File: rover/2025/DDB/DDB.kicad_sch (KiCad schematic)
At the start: 93 parts, among them J1 USB_C_USB4105-GF-A, J2 ETH-RJHSE508104, J3 TerminalBlock, J4 ETH-RJHSE508104, J8 XT30PW-F, SW1 TS09-63-25-WT-160-SMT-TR, SW2 TS09-63-25-WT-160-SMT-TR, U1 ESP32-S3-WROVER, U10 HSS-VN7140ASTR, U11 HSS-VN7140ASTR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

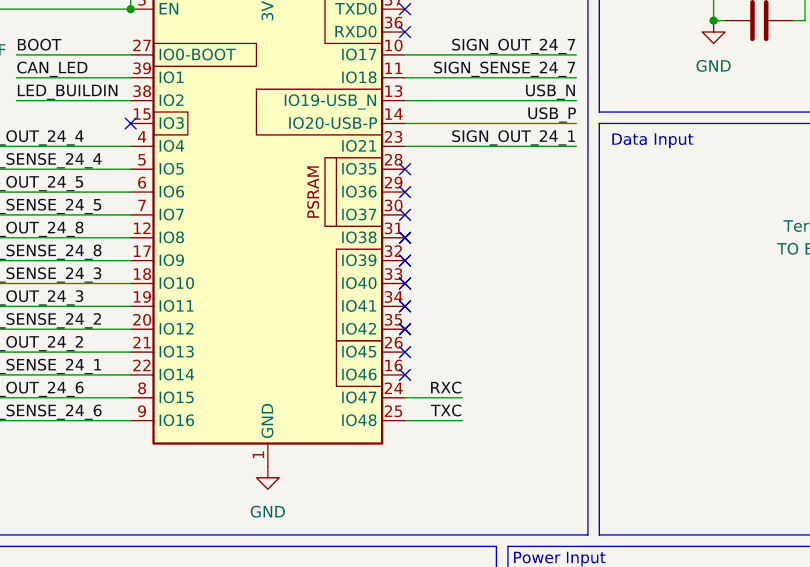
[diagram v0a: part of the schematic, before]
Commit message: Update sch and pcb for correct link
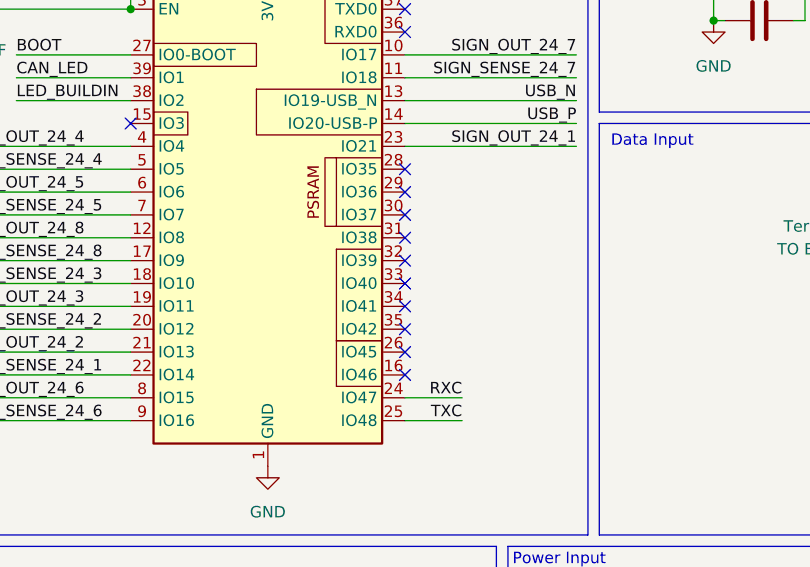
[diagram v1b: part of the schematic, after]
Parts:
- C1: symbol RoverLibrary:C-1uF -> 0_RoverLibrary:C-1uF
- C2: symbol RoverLibrary:C-22uF -> 0_RoverLibrary:C-22uF
- C3, C4, C5, C7: symbol RoverLibrary:C-100nF -> 0_RoverLibrary:C-100nF
- F1, F10, F11, F2, F3, F4, F5, F6, F7, F8: footprint 0_RoverFootprint:FUSE_3568-20 -> RoverFootprint:FUSE_3568-20
- H6, H7: symbol RoverLibrary:MountingHole_Pad -> 0_RoverLibrary:MountingHole_Pad
- R1: symbol RoverLibrary:R-10k -> 0_RoverLibrary:R-10k
- SW1, SW2: symbol RoverLibrary:PushButton-TS09-63-25-WT-160-SMT-TR -> 0_RoverLibrary:PushButton-TS09-63-25-WT-160-SMT-TR
- U1: symbol RoverLibrary:ESP32-S3-WROVER -> 0_RoverLibrary:ESP32-S3-WROVER
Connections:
- no-connect marks 54 -> 49

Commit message: .
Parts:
- U6: value HSS-VN7004SLHTR -> HSS-VN7004SLHTR
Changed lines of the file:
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@@
 	(label "RXC"
 		(at 106.68 72.39 180)
-		(fields_autoplaced yes)
 		(effects
 			(font
@@
 	(label "BOOT"
 		(at 57.15 34.29 0)
-		(fields_autoplaced yes)
 		(effects
 			(font
@@
 	(label "SIGN_SENSE_24_4"
 		(at 50.8 46.99 0)
-		(fields_autoplaced yes)
 		(effects
 			(font
@@
 	(label "CANH"
 		(at 361.95 175.26 180)
-		(fields_autoplaced yes)
 		(effects
 			(font
@@
 	(label "CANL"
 		(at 350.52 39.37 0)
-		(fields_autoplaced yes)
 		(effects
 			(font
@@
 	(label "SIGN_OUT_24_2"
 		(at 20.32 212.09 0)
-		(fields_autoplaced yes)
 		(effects
 			(font
@@
 	(label "SIGN_OUT_24_3"
 		(at 20.32 251.46 0)
-		(fields_autoplaced yes)
 		(effects
 			(font
@@
 	(label "CANH"
 		(at 350.52 62.23 0)
-		(fields_autoplaced yes)
 		(effects
 			(font
@@
 	(label "USB_P"
 		(at 119.38 41.91 180)
-		(fields_autoplaced yes)
 		(effects
 			(font
@@
 	(label "SIGN_OUT_24_8"
 		(at 50.8 54.61 0)
-		(fields_autoplaced yes)
 		(effects
 			(font
@@
 	(label "SIGN_OUT_24_6"
 		(at 50.8 72.39 0)
-		(fields_autoplaced yes)
 		(effects
 			(font
@@
 	(label "SIGN_SENSE_24_3"
 		(at 36.83 254 0)
-		(fields_autoplaced yes)
 		(effects
 			(font
@@
 	(label "CANH"
 		(at 350.52 36.83 0)
-		(fields_autoplaced yes)
 		(effects
 			(font
@@
 	(label "CANH"
 		(at 281.94 87.63 0)
-		(fields_autoplaced yes)
 		(effects
 			(font
@@
 	(label "SIGN_SENSE_24_6"
 		(at 115.57 254 0)
-		(fields_autoplaced yes)
 		(effects
 			(font
@@
 	(label "EN_PB"
 		(at 63.5 26.67 0)
-		(fields_autoplaced yes)
 		(effects
 			(font
@@
 	(label "SIGN_OUT_24_7"
 		(at 119.38 34.29 180)
-		(fields_autoplaced yes)
 		(effects
 			(font
@@
 	(label "SIGN_OUT_24_5"
 		(at 99.06 212.09 0)
-		(fields_autoplaced yes)
 		(effects
 			(font
@@
 	(label "SIGN_OUT_24_7"
 		(at 179.07 173.99 0)
-		(fields_autoplaced yes)
 		(effects
 			(font
@@
 	(label "SIGN_SENSE_24_2"
 		(at 50.8 64.77 0)
-		(fields_autoplaced yes)
 		(effects
 			(font
@@
 	(label "LED_BUILDIN"
 		(at 383.54 162.56 0)
-		(fields_autoplaced yes)
 		(effects
 			(font
@@
 	(label "CANH"
 		(at 281.94 113.03 0)
-		(fields_autoplaced yes)
 		(effects
 			(font
@@
 	(label "SIGN_SENSE_24_5"
 		(at 115.57 214.63 0)
-		(fields_autoplaced yes)
 		(effects
 			(font
@@
 	(label "SIGN_SENSE_24_6"
 		(at 50.8 74.93 0)
-		(fields_autoplaced yes)
 		(effects
 			(font
@@
 	(label "CANL"
 		(at 350.52 64.77 0)
-		(fields_autoplaced yes)
 		(effects
 			(font
@@
 	(label "USB_N"
 		(at 119.38 39.37 180)
-		(fields_autoplaced yes)
 		(effects
 			(font
@@
 	(label "CAN_LED"
 		(at 57.15 36.83 0)
-		(fields_autoplaced yes)
 		(effects
 			(font
@@
 	(label "CAN_LED"
 		(at 368.3 162.56 0)
-		(fields_autoplaced yes)
 		(effects
 			(font
@@
 	(label "SIGN_OUT_24_2"
 		(at 50.8 67.31 0)
-		(fields_autoplaced yes)
 		(effects
 			(font
@@
 	(label "BOOT"
 		(at 152.4 22.86 180)
-		(fields_autoplaced yes)
 		(effects
 			(font
@@
 	(label "SIGN_SENSE_24_1"
 		(at 39.37 176.53 0)
-		(fields_autoplaced yes)
 		(effects
 			(font
@@
 	(label "CANL"
 		(at 361.95 177.8 180)
-		(fields_autoplaced yes)
 		(effects
 			(font
@@
 	(label "EN_PB"
 		(at 187.96 22.86 180)
-		(fields_autoplaced yes)
 		(effects
 			(font
@@
 	(label "SIGN_SENSE_24_5"
 		(at 50.8 52.07 0)
-		(fields_autoplaced yes)
 		(effects
 			(font
@@
 	(label "CANH"
 		(at 162.56 67.31 180)
-		(fields_autoplaced yes)
 		(effects
 			(font
@@
 	(label "SIGN_OUT_24_6"
 		(at 99.06 251.46 0)
-		(fields_autoplaced yes)
 		(effects
 			(font
@@
 	(label "SIGN_SENSE_24_8"
 		(at 195.58 214.63 0)
-		(fields_autoplaced yes)
 		(effects
 			(font
@@
 	(label "CANL"
 		(at 350.52 115.57 0)
-		(fields_autoplaced yes)
 		(effects
 			(font
@@
 	(label "CANH"
 		(at 281.94 36.83 0)
-		(fields_autoplaced yes)
 		(effects
 			(font
@@
 	(label "SIGN_OUT_24_3"
 		(at 50.8 62.23 0)
-		(fields_autoplaced yes)
 		(effects
 			(font
@@
 	(label "SIGN_SENSE_24_3"
 		(at 50.8 59.69 0)
-		(fields_autoplaced yes)
 		(effects
 			(font
@@
 	(label "SIGN_SENSE_24_7"
 		(at 119.38 36.83 180)
-		(fields_autoplaced yes)
 		(effects
 			(font
@@
 	(label "USB_P"
 		(at 52.07 118.11 180)
-		(fields_autoplaced yes)
 		(effects
 			(font
@@
 	(label "SIGN_OUT_24_1"
 		(at 119.38 44.45 180)
-		(fields_autoplaced yes)
 		(effects
 			(font
@@
 	(label "LOW_PW_EN"
 		(at 138.43 113.03 0)
-		(fields_autoplaced yes)
 		(effects
 			(font
@@
 	(label "CANH"
 		(at 281.94 62.23 0)
-		(fields_autoplaced yes)
 		(effects
 			(font
@@
 	(label "SIGN_SENSE_24_1"
 		(at 50.8 69.85 0)
-		(fields_autoplaced yes)
 		(effects
 			(font
@@
 	(label "CANL"
 		(at 281.94 64.77 0)
-		(fields_autoplaced yes)
 		(effects
 			(font
@@
 	(label "SIGN_SENSE_24_7"
 		(at 195.58 176.53 0)
-		(fields_autoplaced yes)
 		(effects
 			(font
@@
 	(label "TXC"
 		(at 106.68 74.93 180)
-		(fields_autoplaced yes)
 		(effects
 			(font
@@
 	(label "USB_P"
 		(at 62.23 106.68 0)
-		(fields_autoplaced yes)
 		(effects
 			(font
@@
 	(label "USB_N"
 		(at 62.23 104.14 0)
-		(fields_autoplaced yes)
 		(effects
 			(font
@@
 	(label "CC1"
 		(at 52.07 105.41 180)
-		(fields_autoplaced yes)
 		(effects
 			(font
@@
 	(label "CC2"
 		(at 52.07 107.95 180)
-		(fields_autoplaced yes)
 		(effects
 			(font
@@
 	(label "CC2"
 		(at 71.12 130.81 0)
-		(fields_autoplaced yes)
 		(effects
 			(font
@@
 	(label "TXC"
 		(at 361.95 172.72 180)
-		(fields_autoplaced yes)
 		(effects
 			(font
@@
 	(label "SIGN_OUT_24_5"
 		(at 50.8 49.53 0)
-		(fields_autoplaced yes)
 		(effects
 			(font
@@
 	(label "CC1"
 		(at 71.12 123.19 0)
-		(fields_autoplaced yes)
 		(effects
 			(font
@@
 	(label "CANH"
 		(at 350.52 87.63 0)
-		(fields_autoplaced yes)
 		(effects
 			(font
@@
 	(label "SIGN_OUT_24_8"
 		(at 179.07 212.09 0)
-		(fields_autoplaced yes)
 		(effects
 			(font
@@
 	(label "CANL"
 		(at 281.94 115.57 0)
-		(fields_autoplaced yes)
 		(effects
 			(font
@@
 	(label "CANL"
 		(at 281.94 39.37 0)
-		(fields_autoplaced yes)
 		(effects
 			(font
@@
 	(label "SIGN_OUT_24_4"
 		(at 100.33 173.99 0)
-		(fields_autoplaced yes)
 		(effects
 			(font
@@
 	(label "LED_BUILDIN"
 		(at 57.15 39.37 0)
-		(fields_autoplaced yes)
 		(effects
 			(font
@@
 	(label "SIGN_SENSE_24_4"
 		(at 116.84 176.53 0)
-		(fields_autoplaced yes)
 		(effects
 			(font
@@
 	(label "CANL"
 		(at 281.94 90.17 0)
-		(fields_autoplaced yes)
 		(effects
 			(font
@@
 	(label "LOW_PW_EN"
 		(at 181.61 59.69 180)
-		(fields_autoplaced yes)
 		(effects
 			(font
@@
 	(label "SIGN_OUT_24_4"
 		(at 50.8 44.45 0)
-		(fields_autoplaced yes)
 		(effects
 			(font
@@
 	(label "RXC"
 		(at 361.95 170.18 180)
-		(fields_autoplaced yes)
 		(effects
 			(font
@@
 	(label "CANH"
 		(at 350.52 113.03 0)
-		(fields_autoplaced yes)
 		(effects
 			(font
@@
 	(label "SIGN_SENSE_24_2"
 		(at 38.1 214.63 0)
-		(fields_autoplaced yes)
 		(effects
 			(font
@@
 	(label "CANL"
 		(at 162.56 64.77 180)
-		(fields_autoplaced yes)
 		(effects
 			(font
@@
 	(label "USB_N"
 		(at 52.07 113.03 180)
-		(fields_autoplaced yes)
 		(effects
 			(font
@@
 	(label "SIGN_SENSE_24_8"
 		(at 50.8 57.15 0)
-		(fields_autoplaced yes)
 		(effects
 			(font
@@
 	(label "CANL"
 		(at 350.52 90.17 0)
-		(fields_autoplaced yes)
 		(effects
 			(font
@@
 	(label "SIGN_OUT_24_1"
 		(at 20.32 173.99 0)
-		(fields_autoplaced yes)
 		(effects
 			(font
@@
 			)
 		)
-		(property "Value" "HSS-VN7004SLHTR "
+		(property "Value" "HSS-VN7004SLHTR"
 			(at 170.18 100.33 0)
 			(effects
